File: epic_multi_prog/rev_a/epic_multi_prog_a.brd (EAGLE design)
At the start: 53.3 x 38.1 mm, 44 parts, among them J1 EPIC-PROG-PORT, J2 MICRO_USB_B_HIROSE_ZX62R-B-5P, J3 MEC1-105-02-XX-XX-D-A, J4 TAG_CONNECT_HEADER_EPIC, J5 MICRO_USB_B_MALE_HIROSE_ZX80-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, U1 FT232RL, U2 MAX1555, U3 MAX1555, U4 MAX1555, U5 MAX1555

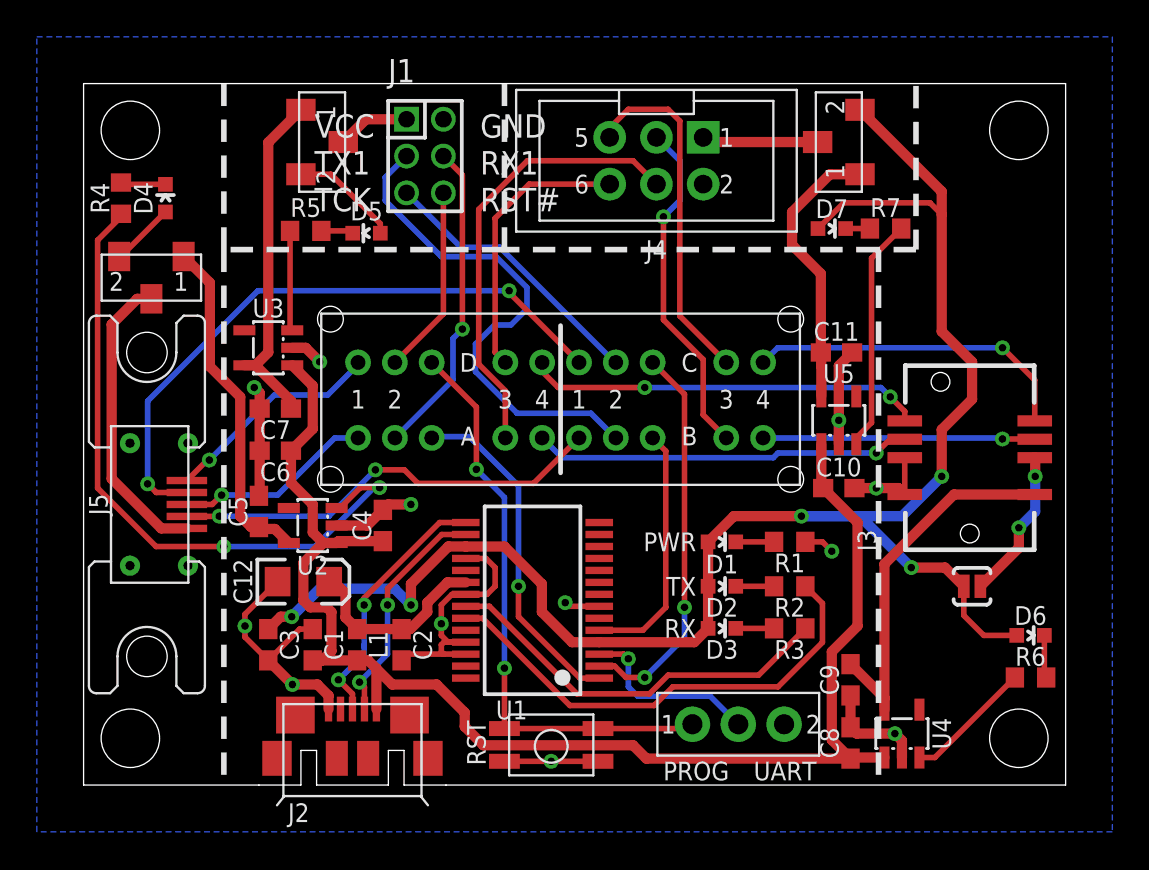
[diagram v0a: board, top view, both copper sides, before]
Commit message: added milling layer for pannelization
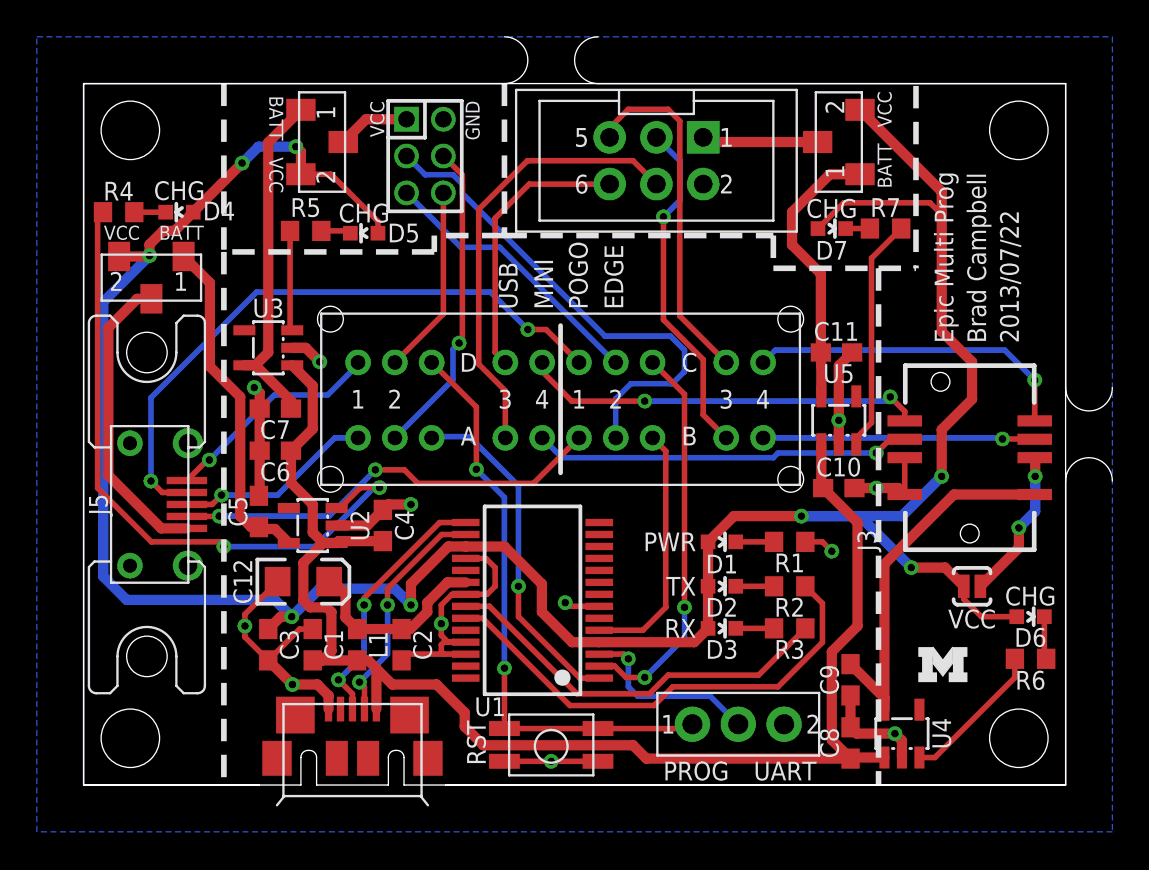
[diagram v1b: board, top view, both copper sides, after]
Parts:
- added U$1: UMICH_SOLID_SMALL, logos:UMICH_SOLID_75MIL
- moved D4 1.08 mm to (5.21, 31.1), turned to 90 degrees
- moved D6 1.02 mm to (51.4, 9.14)
- moved R6 1.02 mm to (51.4, 6.86)
- moved R4 0.77 mm to (1.91, 31.1), turned to 180 degrees
- moved D5 0.13 mm to (15.2, 30.0)
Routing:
- net 3V3: track 104.8 -> 144.0 mm, vias 5 -> 8
- net N$19: track 6.99 -> 8.00 mm
- net N$9: track 2.43 -> 1.70 mm
- net TX_MINIPROG: track 27.9 -> 27.4 mm
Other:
- board size 53.3 x 38.1 mm -> 55.9 x 40.6 mm
- board text added: "2013/07/22"
- board text added: "BATT"
- board text added: "Brad Campbell"
- board text added: "CHG"
- board text added: "EDGE"
- board text added: "Epic Multi Prog"
- board text added: "GND"
- board text added: "MINI"
- board text added: "POGO"
- board text added: "USB"
- board text added: "VCC"
